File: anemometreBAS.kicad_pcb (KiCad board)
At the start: 2 copper layers, 77 x 50 mm, 15 parts, among them U1 TP4056

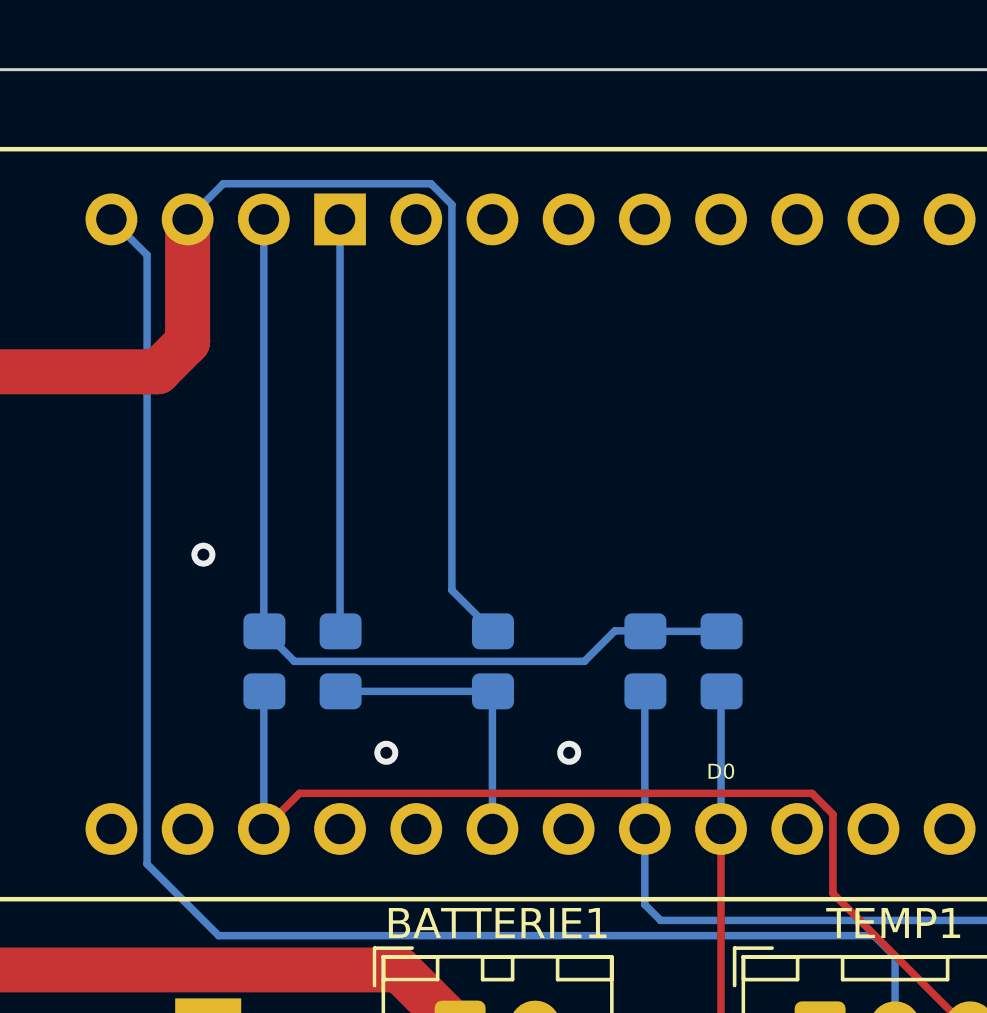
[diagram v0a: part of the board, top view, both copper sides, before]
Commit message: pcb without smd resistor first routing version
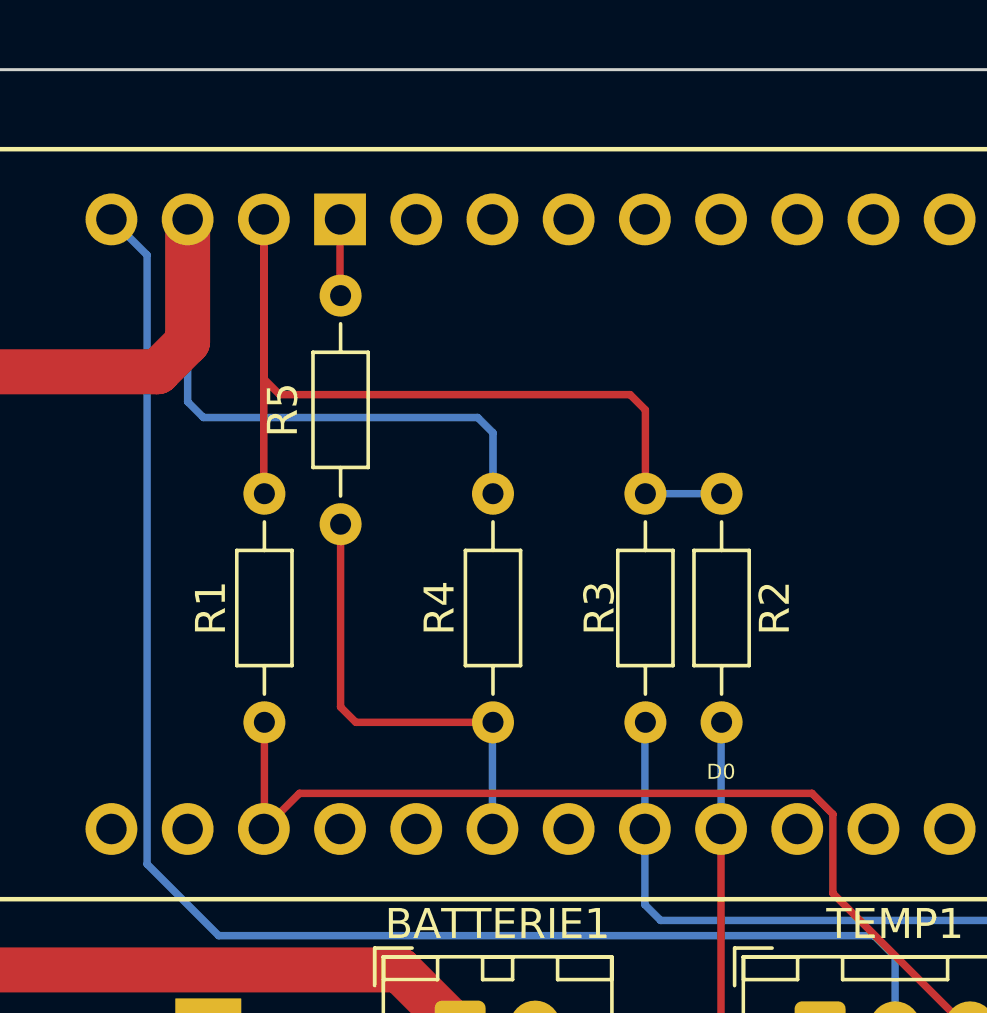
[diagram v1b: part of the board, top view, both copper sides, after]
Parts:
- R1, R2, R3, R4, R5: footprint Resistor_SMD:R_0805_2012Metric_Pad1.20x1.40mm_HandSolder -> Resistor_THT:R_Axial_DIN0204_L3.6mm_D1.6mm_P7.62mm_Horizontal; moved to F.Cu
- moved R1 5.59 mm to (125.5, 70.1)
- moved R3 5.59 mm to (138.2, 70.1)
- moved R4 5.59 mm to (133.1, 70.1)
- moved R5 4.57 mm to (128.0, 71.1)
- moved R2 2.03 mm to (140.7, 77.7)
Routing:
- net GND: track 13.7 -> 2.55 mm, vias 3 -> 0
- net VIN: track 69.6 -> 63.9 mm
- net VBridgeBat: track 9.68 -> 14.9 mm
- net 3V3: track 29.8 -> 32.9 mm
- net Net-(ANEMO1-Pad2): track 23.7 -> 22.7 mm
- net VBridgeDir: track 32.8 -> 31.7 mm
- net Net-(R1-Pad2): track 33.5 -> 32.4 mm

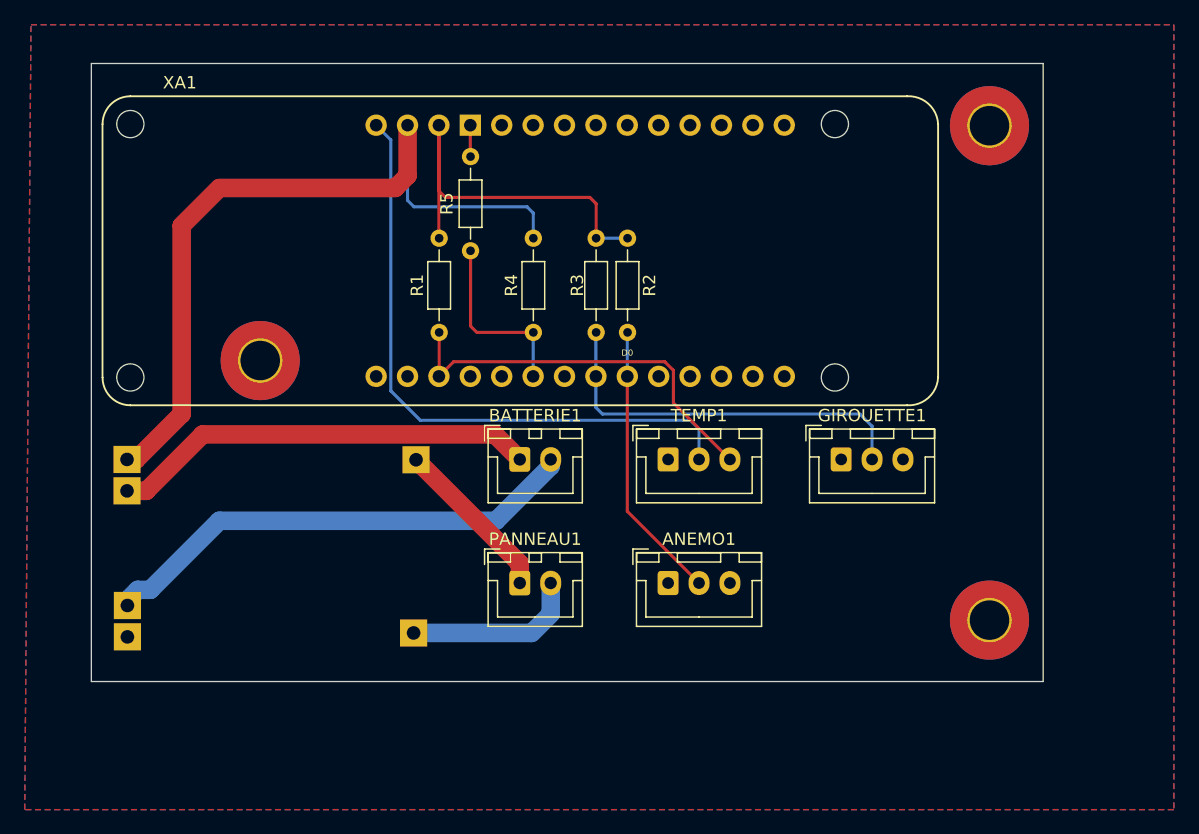
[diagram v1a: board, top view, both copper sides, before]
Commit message: change layer of solar panel and battery mngt card unshow $Reference and value
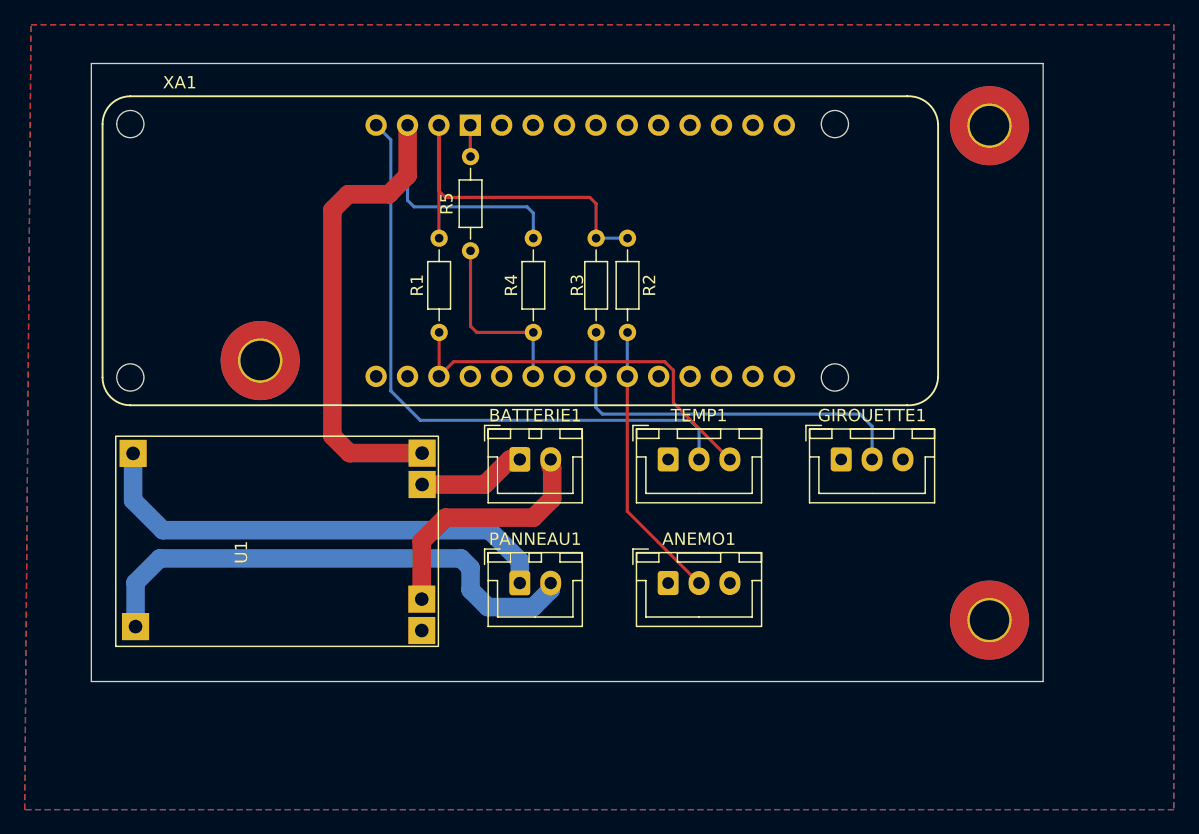
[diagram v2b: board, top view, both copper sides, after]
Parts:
- U1: moved to F.Cu
- moved U1 25.7 mm to (99.3, 103.1)
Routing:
- net Net-(PANNEAU1-Pad2): track 14.2 -> 41.8 mm
- net Net-(BATTERIE1-Pad1): track 34.5 -> 8.74 mm
- net Net-(PANNEAU1-Pad1): track 13.5 -> 38.9 mm
- net Net-(BATTERIE1-Pad2): track 39.7 -> 19.9 mm
- net VIN: track 63.9 -> 56.1 mm
